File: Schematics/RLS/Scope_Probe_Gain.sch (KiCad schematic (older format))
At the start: 12 parts, among them J1 Velleman_Probe1, J2 Velleman_Probe2, J3 Velleman_FuncGen, U12 ULN2803A, U13 R70-5D1-3, U14 R70-5D1-3

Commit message: Lots of changes
Completed Schematic
1/3 Done PCB
Multisim file for testing ADC protection and buffer circuit
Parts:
- removed U13, U14: R70-5D1-3, symbol R70-5D1-3
- added U13, U14: RA30421051, RLS_CustomFootprints:DIP-8(14)_W7.62mm, symbol RA30421051
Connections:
- net +5V: now also U13.2 (VCC), U14.2 (VCC)
- net POS_SCP1: now also U13.1 (SW1)
- net POS_SCP2: now also C2.1, R18.2, U14.1 (SW1); no longer C2.2, R18.1
- net RLY1: now also U13.3 (Toggle)
- net RLY2: now also U14.3 (Toggle)
- net +SCP1: now reaches J1.3 (P3)
- net +SCP1: now also U13.4 (SW_In)
- net SCP1_10X: now reaches C1.1, R17.2
- net SCP1_10X: now also U13.8 (SW2)
- net +SCP2: now reaches J2.3 (P3)
- net +SCP2: now also U14.4 (SW_In)
- new net SCP2_10X: C2.2, R18.1, U14.8 (SW2)
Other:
- moved on the sheet: C1, C2, J1, J2, J3, R17, R18
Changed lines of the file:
@@
 LIBS:valves
 LIBS:arduino_shield
-LIBS:arduino_shieldsNCL
+LIBS:RA30421051
+LIBS:RB496EATR
+LIBS:Daughterboard_Connector
 LIBS:RLS-cache
 EELAYER 25 0
@@
 Text GLabel 4850 1700 2    60   Input ~ 0
 RLY2
-$Comp
-L R70-5D1-3 U13
-U 1 1 595850A9
-P 7250 1800
-F 0 "U13" H 7350 2000 60  0000 C CNN
-F 1 "R70-5D1-3" V 7100 2000 60  0000 C CNN
-F 2 "" H 7250 1800 60  0001 C CNN
-F 3 "" H 7250 1800 60  0001 C CNN
-	1    7250 1800
-	-1   0    0    -1
-$EndComp
-$Comp
-L R70-5D1-3 U14
-U 1 1 59585156
-P 7200 3150
-F 0 "U14" H 7300 3350 60  0000 C CNN
-F 1 "R70-5D1-3" V 7050 3350 60  0000 C CNN
-F 2 "" H 7200 3150 60  0001 C CNN
-F 3 "" H 7200 3150 60  0001 C CNN
-	1    7200 3150
-	-1   0    0    -1
-$EndComp
-Text GLabel 6050 1600 0    60   Input ~ 0
+Text GLabel 7100 1100 1    60   Input ~ 0
 POS_SCP1
-Text GLabel 6050 2950 0    60   Input ~ 0
+Text GLabel 9350 1050 1    60   Input ~ 0
 POS_SCP2
-Text GLabel 7500 2300 0    60   Input ~ 0
+Text GLabel 6350 3500 0    60   Input ~ 0
 NEG_SCP1
-Text GLabel 7400 3700 0    60   Input ~ 0
+Text GLabel 8700 3500 0    60   Input ~ 0
 NEG_SCP2
 $Comp
 L R R17
 U 1 1 595881BF
-P 6600 1850
-F 0 "R17" V 6680 1850 50  0000 C CNN
-F 1 "9M" V 6600 1850 50  0000 C CNN
-F 2 "Resistors_THT:R_Axial_DIN0309_L9.0mm_D3.2mm_P12.70mm_Horizontal" V 6530 1850 50  0001 C CNN
-F 3 "" H 6600 1850 50  0001 C CNN
-	1    6600 1850
-	0    -1   -1   0
+P 7700 1400
+F 0 "R17" V 7780 1400 50  0000 C CNN
+F 1 "9M" V 7700 1400 50  0000 C CNN
+F 2 "Resistors_THT:R_Axial_DIN0309_L9.0mm_D3.2mm_P12.70mm_Horizontal" V 7630 1400 50  0001 C CNN
+F 3 "" H 7700 1400 50  0001 C CNN
+	1    7700 1400
+	1    0    0    -1
 $EndComp
 $Comp
 L R R18
 U 1 1 59588224
-P 6550 3200
-F 0 "R18" V 6630 3200 50  0000 C CNN
-F 1 "9M" V 6550 3200 50  0000 C CNN
-F 2 "Resistors_THT:R_Axial_DIN0309_L9.0mm_D3.2mm_P12.70mm_Horizontal" V 6480 3200 50  0001 C CNN
-F 3 "" H 6550 3200 50  0001 C CNN
-	1    6550 3200
-	0    -1   -1   0
+P 10050 1500
+F 0 "R18" V 10130 1500 50  0000 C CNN
+F 1 "9M" V 10050 1500 50  0000 C CNN
+F 2 "Resistors_THT:R_Axial_DIN0309_L9.0mm_D3.2mm_P12.70mm_Horizontal" V 9980 1500 50  0001 C CNN
+F 3 "" H 10050 1500 50  0001 C CNN
+	1    10050 1500
+	-1   0    0    1
 $EndComp
 $Comp
 L C_Small C1
 U 1 1 595882C2
-P 6600 2050
-F 0 "C1" H 6610 2120 50  0000 L CNN
-F 1 "15pF" H 6610 1970 50  0000 L CNN
-F 2 "Capacitors_THT:C_Disc_D3.8mm_W2.6mm_P2.50mm" H 6600 2050 50  0001 C CNN
-F 3 "" H 6600 2050 50  0001 C CNN
-	1    6600 2050
-	0    1    1    0
+P 7500 1400
+F 0 "C1" H 7510 1470 50  0000 L CNN
+F 1 "15pF" H 7510 1320 50  0000 L CNN
+F 2 "Capacitors_THT:C_Disc_D3.8mm_W2.6mm_P2.50mm" H 7500 1400 50  0001 C CNN
+F 3 "" H 7500 1400 50  0001 C CNN
+	1    7500 1400
+	-1   0    0    1
 $EndComp
 $Comp
 L C_Small C2
 U 1 1 595883A5
+P 10250 1500
+F 0 "C2" H 10260 1570 50  0000 L CNN
+F 1 "15pF" H 10260 1420 50  0000 L CNN
+F 2 "Capacitors_THT:C_Disc_D3.8mm_W2.6mm_P2.50mm" H 10250 1500 50  0001 C CNN
+F 3 "" H 10250 1500 50  0001 C CNN
+	1    10250 1500
+	1    0    0    -1
+$EndComp
+$Comp
+L CONN_01X03 J1
+U 1 1 595883FC
 P 6550 3400
-F 0 "C2" H 6560 3470 50  0000 L CNN
-F 1 "15pF" H 6560 3320 50  0000 L CNN
-F 2 "Capacitors_THT:C_Disc_D3.8mm_W2.6mm_P2.50mm" H 6550 3400 50  0001 C CNN
+F 0 "J1" H 6550 3600 50  0000 C CNN
+F 1 "Velleman_Probe1" V 6650 3400 50  0000 C CNN
+F 2 "Pin_Headers:Pin_Header_Straight_1x03_Pitch2.54mm" H 6550 3400 50  0001 C CNN
 F 3 "" H 6550 3400 50  0001 C CNN
 	1    6550 3400
-	0    1    1    0
-$EndComp
-$Comp
-L CONN_01X03 J1
-U 1 1 595883FC
-P 7700 2200
-F 0 "J1" H 7700 2400 50  0000 C CNN
-F 1 "Velleman_Probe1" V 7800 2200 50  0000 C CNN
-F 2 "Pin_Headers:Pin_Header_Straight_1x03_Pitch2.54mm" H 7700 2200 50  0001 C CNN
-F 3 "" H 7700 2200 50  0001 C CNN
-	1    7700 2200
 	1    0    0    1
 $EndComp
@@
 L CONN_01X03 J2
 U 1 1 5958858D
-P 7600 3600
-F 0 "J2" H 7600 3800 50  0000 C CNN
-F 1 "Velleman_Probe2" V 7700 3600 50  0000 C CNN
-F 2 "Pin_Headers:Pin_Header_Straight_1x03_Pitch2.54mm" H 7600 3600 50  0001 C CNN
-F 3 "" H 7600 3600 50  0001 C CNN
-	1    7600 3600
+P 8900 3400
+F 0 "J2" H 8900 3600 50  0000 C CNN
+F 1 "Velleman_Probe2" V 9000 3400 50  0000 C CNN
+F 2 "Pin_Headers:Pin_Header_Straight_1x03_Pitch2.54mm" H 8900 3400 50  0001 C CNN
+F 3 "" H 8900 3400 50  0001 C CNN
+	1    8900 3400
 	1    0    0    1
 $EndComp
-NoConn ~ 7250 2700
-NoConn ~ 7300 1350
-Text GLabel 7050 2700 1    60   Input ~ 0
+Text GLabel 8750 2750 0    60   Input ~ 0
 RLY2
-Text GLabel 7100 1350 1    60   Input ~ 0
+Text GLabel 6400 2700 0    60   Input ~ 0
 RLY1
-Text GLabel 7100 1850 3    60   Input ~ 0
+Text GLabel 8750 2150 0    60   Input ~ 0
 +5V
-Text GLabel 7050 3200 3    60   Input ~ 0
+Text GLabel 6400 2100 0    60   Input ~ 0
 +5V
-Wire Wire Line
-	4850 2400 5300 2400
-Wire Wire Line
-	5300 2400 5300 950
-Wire Wire Line
-	5300 950  3350 950
-Wire Wire Line
-	3700 1400 3700 1700
-Wire Wire Line
-	3250 1700 4050 1700
-Wire Wire Line
-	3250 1600 4050 1600
-Wire Wire Line
-	3500 1400 3500 1600
-Wire Wire Line
-	3500 1100 3500 950
-Connection ~ 3500 950
-Wire Wire Line
-	3700 1100 3700 950
-Connection ~ 3700 950
-Connection ~ 3500 1600
-Connection ~ 3700 1700
-Wire Wire Line
-	7500 2100 7300 2100
-Wire Wire Line
-	7300 2100 7300 1850
-Wire Wire Line
-	7400 3500 7250 3500
-Wire Wire Line
-	7250 3500 7250 3200
-Wire Wire Line
-	6700 3200 6950 3200
-Wire Wire Line
-	6800 3200 6800 3400
-Wire Wire Line
-	6800 3400 6650 3400
-Connection ~ 6800 3200
-Wire Wire Line
-	6200 3200 6400 3200
-Wire Wire Line
-	6300 3200 6300 3400
-Wire Wire Line
-	6300 3400 6450 3400
-Wire Wire Line
-	6950 2700 6200 2700
-Wire Wire Line
-	6200 2700 6200 3200
-Connection ~ 6300 3200
-Wire Wire Line
-	6200 2950 6050 2950
-Connection ~ 6200 2950
-Wire Wire Line
-	6750 1850 7000 1850
-Wire Wire Line
-	6850 1850 6850 2050
-Wire Wire Line
-	6850 2050 6700 2050
-Connection ~ 6850 1850
-Wire Wire Line
-	6200 1850 6450 1850
-Wire Wire Line
-	6300 1850 6300 2050
-Wire Wire Line
-	6300 2050 6500 2050
-Wire Wire Line
-	6200 1350 6200 1850
-Wire Wire Line
-	6200 1350 7000 1350
-Connection ~ 6300 1850
-Wire Wire Line
-	6200 1600 6050 1600
-Connection ~ 6200 1600
 $Comp
 L CONN_01X03 J3
 U 1 1 595A5435
-P 8650 2800
-F 0 "J3" H 8650 3000 50  0000 C CNN
-F 1 "Velleman_FuncGen" V 8750 2800 50  0000 C CNN
-F 2 "Pin_Headers:Pin_Header_Straight_1x03_Pitch2.54mm" H 8650 2800 50  0001 C CNN
-F 3 "" H 8650 2800 50  0001 C CNN
-	1    8650 2800
+P 7650 4350
+F 0 "J3" H 7650 4550 50  0000 C CNN
+F 1 "Velleman_FuncGen" V 7750 4350 50  0000 C CNN
+F 2 "Pin_Headers:Pin_Header_Straight_1x03_Pitch2.54mm" H 7650 4350 50  0001 C CNN
+F 3 "" H 7650 4350 50  0001 C CNN
+	1    7650 4350
 	1    0    0    1
 $EndComp
-Text GLabel 8450 2700 0    60   Input ~ 0
+Text GLabel 7450 4250 0    60   Input ~ 0
 POS_GEN
-Text GLabel 8450 2900 0    60   Input ~ 0
+Text GLabel 7450 4450 0    60   Input ~ 0
 NEG_GEN
 NoConn ~ 4850 1800
@@
 NoConn ~ 4050 1900
 NoConn ~ 4050 1800
-NoConn ~ 7400 3600
-NoConn ~ 8450 2800
-NoConn ~ 7500 2200
+NoConn ~ 8700 3400
+NoConn ~ 7450 4350
+NoConn ~ 6350 3400
+$Comp
+L RA30421051 U13
+U 1 1 5962B7F2
+P 7050 1850
+F 0 "U13" H 7050 1950 60  0000 C CNN
+F 1 "RA30421051" H 7050 650 60  0000 C CNN
+F 2 "RLS_CustomFootprints:DIP-8(14)_W7.62mm" H 7050 1850 60  0001 C CNN
+F 3 "" H 7050 1850 60  0001 C CNN
+	1    7050 1850
+	1    0    0    -1
+$EndComp
+$Comp
+L RA30421051 U14
+U 1 1 5962B85D
+P 9400 1900
+F 0 "U14" H 9400 2000 60  0000 C CNN
+F 1 "RA30421051" H 9400 700 60  0000 C CNN
+F 2 "RLS_CustomFootprints:DIP-8(14)_W7.62mm" H 9400 1900 60  0001 C CNN
+F 3 "" H 9400 1900 60  0001 C CNN
+	1    9400 1900
+	1    0    0    -1
+$EndComp
+NoConn ~ 10050 2900
+NoConn ~ 7700 2850
+Wire Wire Line
+	4850 2400 5300 2400
+Wire Wire Line
+	5300 2400 5300 950
+Wire Wire Line
+	5300 950  3350 950
+Wire Wire Line
+	3700 1400 3700 1700
+Wire Wire Line
+	3250 1700 4050 1700
+Wire Wire Line
+	3250 1600 4050 1600
+Wire Wire Line
+	3500 1400 3500 1600
+Wire Wire Line
+	3500 1100 3500 950
+Connection ~ 3500 950
+Wire Wire Line
+	3700 1100 3700 950
+Connection ~ 3700 950
+Connection ~ 3500 1600
+Connection ~ 3700 1700
+Wire Wire Line
+	10050 1100 10050 1350
+Wire Wire Line
+	10050 1250 10250 1250
+Wire Wire Line
+	10250 1250 10250 1400
+Connection ~ 10050 1250
+Wire Wire Line
+	10050 1650 10050 2000
+Wire Wire Line
+	10050 1750 10250 1750
+Wire Wire Line
+	10250 1750 10250 1600
+Connection ~ 10050 1750
+Wire Wire Line
+	8700 3300 8650 3300
+Wire Wire Line
+	8650 3300 8650 2900
+Wire Wire Line
+	8650 2900 8750 2900
+Wire Wire Line
+	6350 3300 6300 3300
+Wire Wire Line
+	6300 3300 6300 2850
+Wire Wire Line
+	6300 2850 6400 2850
+Wire Wire Line
+	6400 1950 6400 1150
+Wire Wire Line
+	6400 1150 7700 1150
+Wire Wire Line
+	7700 1150 7700 1250
+Wire Wire Line
+	7500 1300 7500 1200
+Wire Wire Line
+	7500 1200 7700 1200
+Connection ~ 7700 1200
+Wire Wire Line
+	7700 1550 7700 1950
+Wire Wire Line
+	7500 1500 7500 1600
+Wire Wire Line
+	7500 1600 7700 1600
+Connection ~ 7700 1600
+Connection ~ 7100 1150
+Wire Wire Line
+	7100 1100 7100 1150
+Wire Wire Line
+	8750 2000 8750 1100
+Wire Wire Line
+	8750 1100 10050 1100
+Wire Wire Line
+	9350 1050 9350 1100
+Connection ~ 9350 1100
+Text Label 6300 2950 3    40   ~ 0
++SCP1
+Text Label 7700 1700 0    40   ~ 0
+SCP1_10X
+Text Label 8650 3150 1    40   ~ 0
++SCP2
+Text Label 10050 1850 0    40   ~ 0
+SCP2_10X
 $EndSCHEMATC

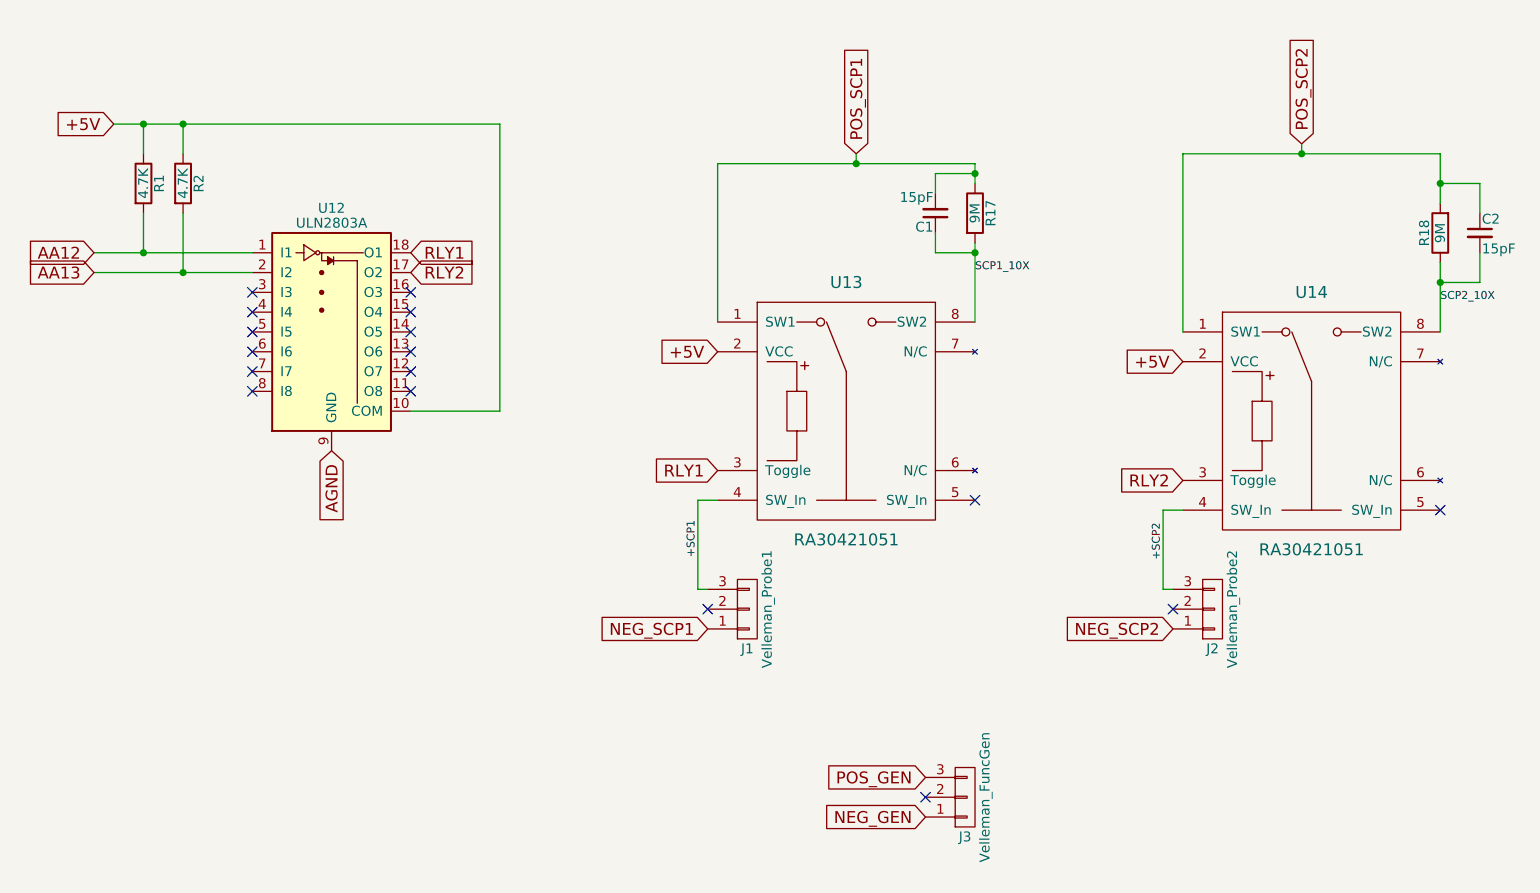
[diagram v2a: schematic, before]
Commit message: Finished PCB but...
Somehow managed to break the schematic file. I know how to fix it, but it is tedious and pointless for now (one has to go through every single individual component and verify that it is the same in the PCB, since the annotation script fucked everything up in the schematic, and therefore any new Netlist).
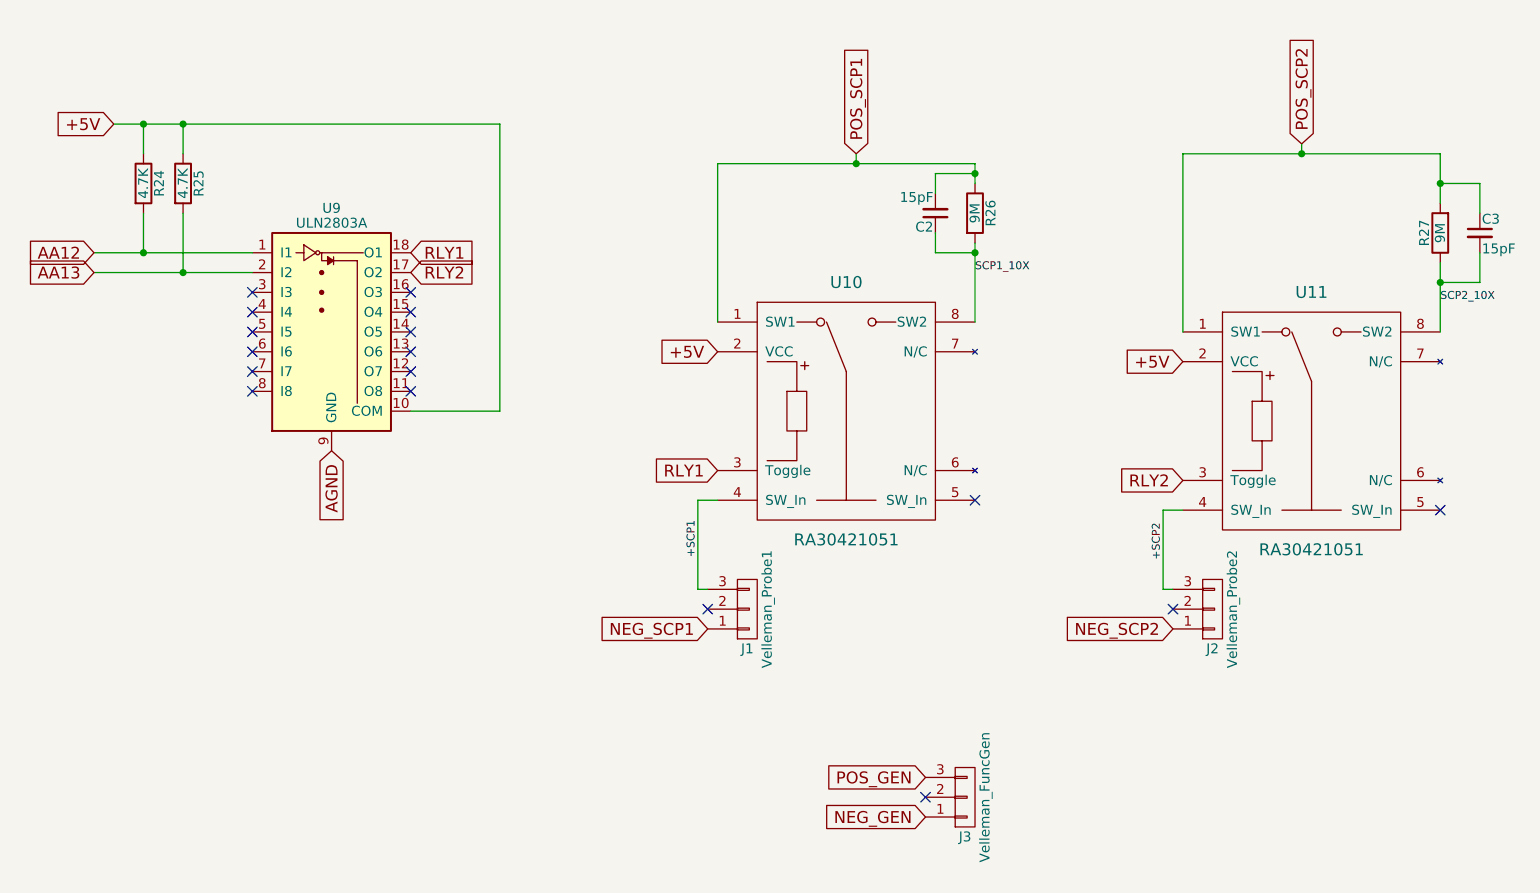
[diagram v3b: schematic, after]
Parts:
- renumbered C1 to C2, C2 to C3, R1 to R24, R2 to R25, R17 to R26, R18 to R27, U13 to U10, U14 to U11, U12 to U9
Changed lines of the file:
@@
 $EndDescr
 $Comp
-L ULN2803A U12
+L ULN2803A U9
 U 1 1 594DCBE5
 P 4450 1900
-F 0 "U12" H 4450 2425 50  0000 C CNN
+F 0 "U9" H 4450 2425 50  0000 C CNN
 F 1 "ULN2803A" H 4450 2350 50  0000 C CNN
 F 2 "Housings_DIP:DIP-18_W7.62mm" H 4500 1250 50  0001 L CNN
@@
 AA13
 $Comp
-L R R1
+L R R24
 U 1 1 594DCDC0
 P 3500 1250
-F 0 "R1" V 3580 1250 50  0000 C CNN
+F 0 "R24" V 3580 1250 50  0000 C CNN
 F 1 "4.7K" V 3500 1250 50  0000 C CNN
 F 2 "Resistors_SMD:R_0805_HandSoldering" V 3430 1250 50  0001 C CNN
@@
 $EndComp
 $Comp
-L R R2
+L R R25
 U 1 1 594DCE13
 P 3700 1250
-F 0 "R2" V 3780 1250 50  0000 C CNN
+F 0 "R25" V 3780 1250 50  0000 C CNN
 F 1 "4.7K" V 3700 1250 50  0000 C CNN
 F 2 "Resistors_SMD:R_0805_HandSoldering" V 3630 1250 50  0001 C CNN
@@
 NEG_SCP2
 $Comp
-L R R17
+L R R26
 U 1 1 595881BF
 P 7700 1400
-F 0 "R17" V 7780 1400 50  0000 C CNN
+F 0 "R26" V 7780 1400 50  0000 C CNN
 F 1 "9M" V 7700 1400 50  0000 C CNN
 F 2 "Resistors_THT:R_Axial_DIN0309_L9.0mm_D3.2mm_P12.70mm_Horizontal" V 7630 1400 50  0001 C CNN
@@
 $EndComp
 $Comp
-L R R18
+L R R27
 U 1 1 59588224
 P 10050 1500
-F 0 "R18" V 10130 1500 50  0000 C CNN
+F 0 "R27" V 10130 1500 50  0000 C CNN
 F 1 "9M" V 10050 1500 50  0000 C CNN
 F 2 "Resistors_THT:R_Axial_DIN0309_L9.0mm_D3.2mm_P12.70mm_Horizontal" V 9980 1500 50  0001 C CNN
@@
 $EndComp
 $Comp
-L C_Small C1
+L C_Small C2
 U 1 1 595882C2
 P 7500 1400
-F 0 "C1" H 7510 1470 50  0000 L CNN
+F 0 "C2" H 7510 1470 50  0000 L CNN
 F 1 "15pF" H 7510 1320 50  0000 L CNN
 F 2 "Capacitors_THT:C_Disc_D3.8mm_W2.6mm_P2.50mm" H 7500 1400 50  0001 C CNN
@@
 $EndComp
 $Comp
-L C_Small C2
+L C_Small C3
 U 1 1 595883A5
 P 10250 1500
-F 0 "C2" H 10260 1570 50  0000 L CNN
+F 0 "C3" H 10260 1570 50  0000 L CNN
 F 1 "15pF" H 10260 1420 50  0000 L CNN
 F 2 "Capacitors_THT:C_Disc_D3.8mm_W2.6mm_P2.50mm" H 10250 1500 50  0001 C CNN
@@
 NoConn ~ 6350 3400
 $Comp
-L RA30421051 U13
+L RA30421051 U10
 U 1 1 5962B7F2
 P 7050 1850
-F 0 "U13" H 7050 1950 60  0000 C CNN
+F 0 "U10" H 7050 1950 60  0000 C CNN
 F 1 "RA30421051" H 7050 650 60  0000 C CNN
 F 2 "RLS_CustomFootprints:DIP-8(14)_W7.62mm" H 7050 1850 60  0001 C CNN
@@
 $EndComp
 $Comp
-L RA30421051 U14
+L RA30421051 U11
 U 1 1 5962B85D
 P 9400 1900
-F 0 "U14" H 9400 2000 60  0000 C CNN
+F 0 "U11" H 9400 2000 60  0000 C CNN
 F 1 "RA30421051" H 9400 700 60  0000 C CNN
 F 2 "RLS_CustomFootprints:DIP-8(14)_W7.62mm" H 9400 1900 60  0001 C CNN

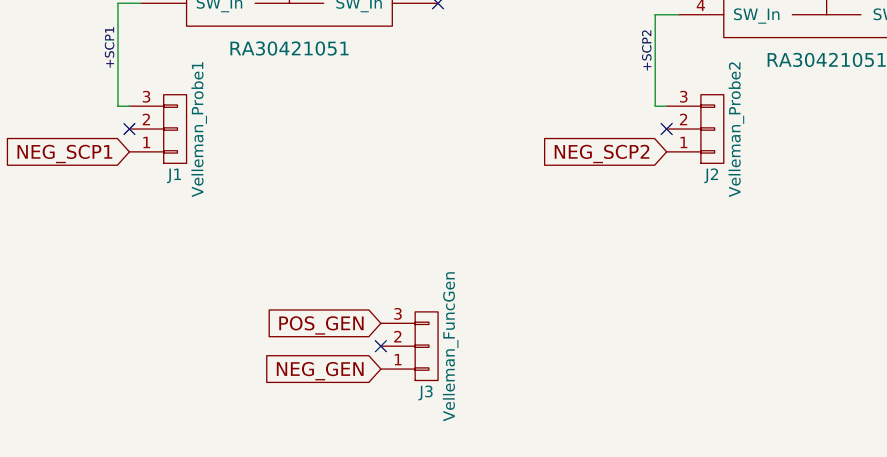
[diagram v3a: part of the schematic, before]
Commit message: Added Things and Fixed Schematic
Added pots to schematic and pcb for adc balancing.
Fixed the component annotation and netlist in the pcb.
Shrunk the pcb down a bit.
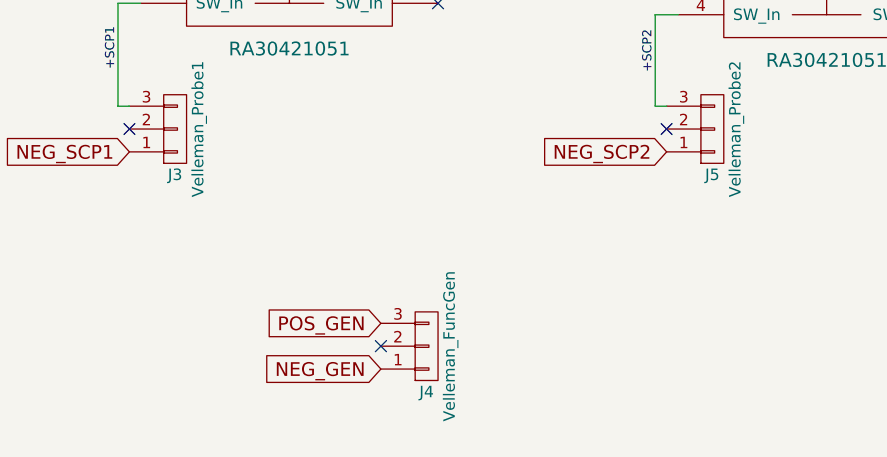
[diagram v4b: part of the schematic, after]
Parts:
- renumbered J1 to J3, J3 to J4, J2 to J5
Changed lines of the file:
@@
 $EndComp
 $Comp
-L CONN_01X03 J1
+L CONN_01X03 J3
 U 1 1 595883FC
 P 6550 3400
-F 0 "J1" H 6550 3600 50  0000 C CNN
+F 0 "J3" H 6550 3600 50  0000 C CNN
 F 1 "Velleman_Probe1" V 6650 3400 50  0000 C CNN
 F 2 "Pin_Headers:Pin_Header_Straight_1x03_Pitch2.54mm" H 6550 3400 50  0001 C CNN
@@
 $EndComp
 $Comp
-L CONN_01X03 J2
+L CONN_01X03 J5
 U 1 1 5958858D
 P 8900 3400
-F 0 "J2" H 8900 3600 50  0000 C CNN
+F 0 "J5" H 8900 3600 50  0000 C CNN
 F 1 "Velleman_Probe2" V 9000 3400 50  0000 C CNN
 F 2 "Pin_Headers:Pin_Header_Straight_1x03_Pitch2.54mm" H 8900 3400 50  0001 C CNN
@@
 +5V
 $Comp
-L CONN_01X03 J3
+L CONN_01X03 J4
 U 1 1 595A5435
 P 7650 4350
-F 0 "J3" H 7650 4550 50  0000 C CNN
+F 0 "J4" H 7650 4550 50  0000 C CNN
 F 1 "Velleman_FuncGen" V 7750 4350 50  0000 C CNN
 F 2 "Pin_Headers:Pin_Header_Straight_1x03_Pitch2.54mm" H 7650 4350 50  0001 C CNN
